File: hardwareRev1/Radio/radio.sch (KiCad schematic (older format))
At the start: 38 parts

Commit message: finaly back on track
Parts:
- removed C?: 2.2pf, symbol C
- removed C?: 22pf, symbol C
- removed C?: 33pf, symbol C
- removed C?: 47pf, symbol C
- removed C?: 15pf, symbol C
- removed C?: 4.7pf, symbol C
- removed C?: 1.8pf, symbol C
- removed C? (x4): C, symbol C
- removed L?: 150nh, symbol INDUCTOR
- removed L?: 120nH, symbol INDUCTOR
- removed L?: 39nH, symbol INDUCTOR
- removed L?: 47nH, symbol INDUCTOR
- removed L?: INDUCTOR, symbol INDUCTOR
- removed R?: R, symbol R
- removed U?: RF5110G, MODULE, symbol RF5110G
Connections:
- wire segments 107 -> 68

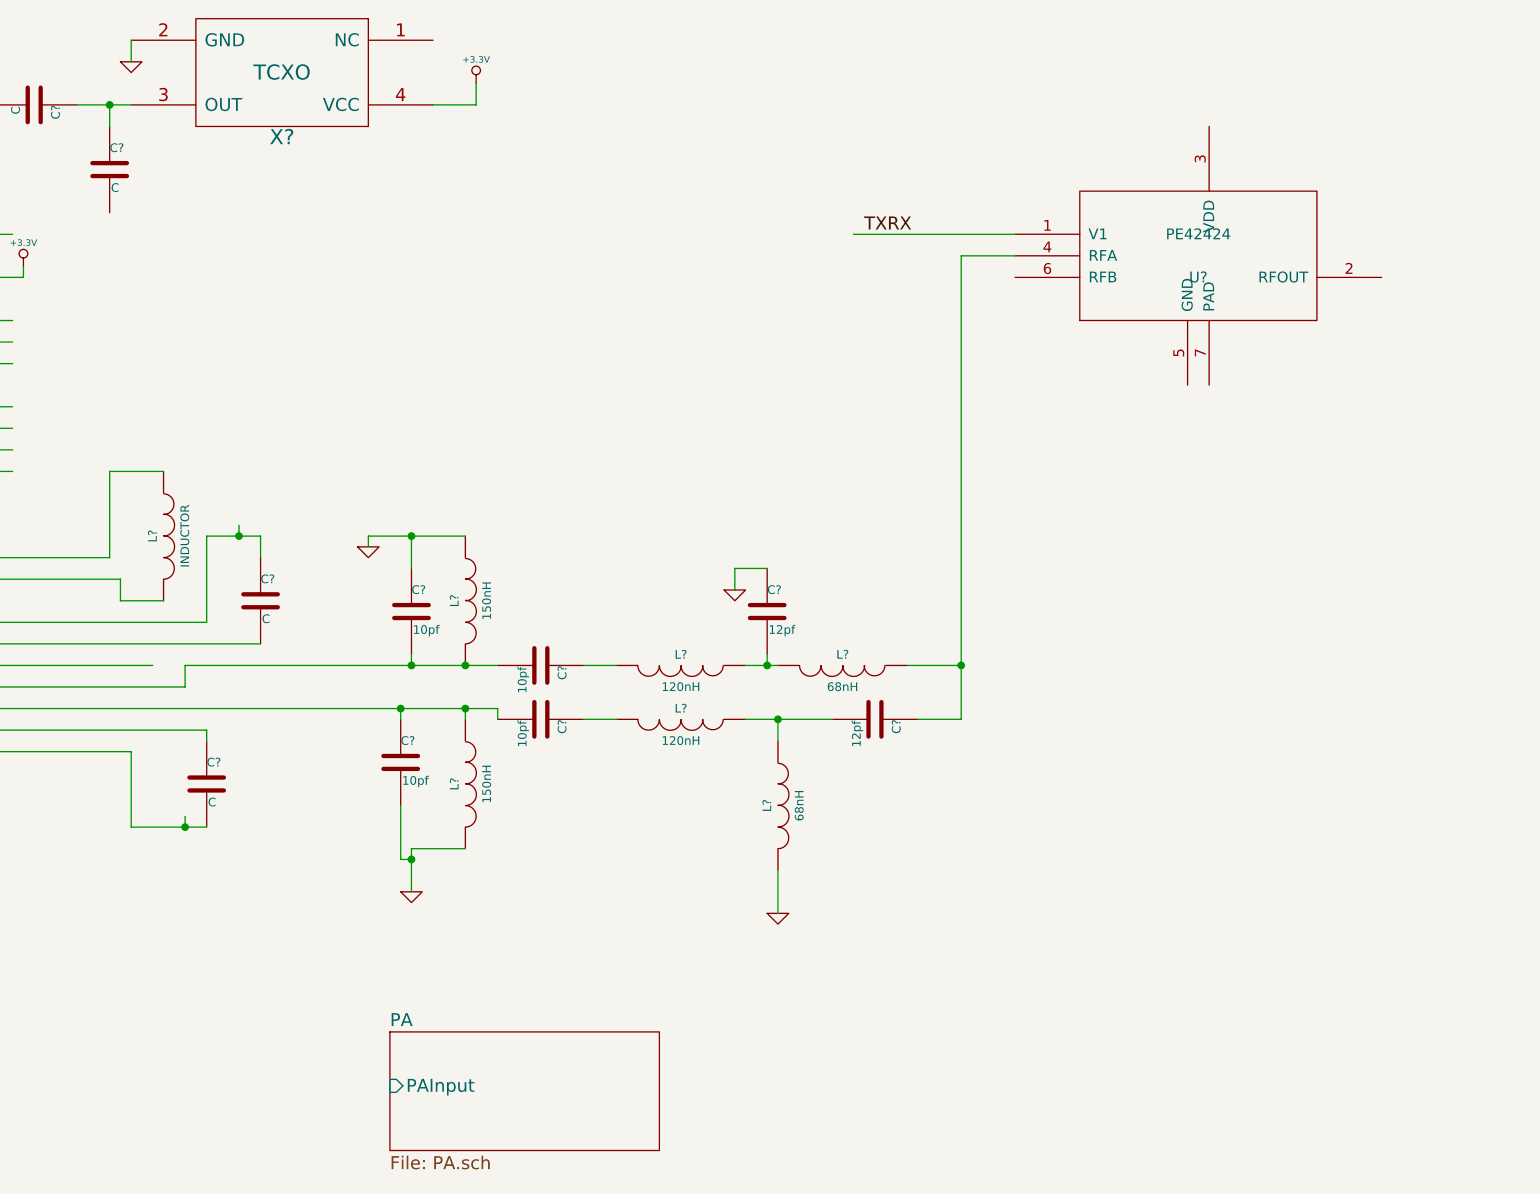
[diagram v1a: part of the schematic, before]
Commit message: Added the outline for the RF module. Also finished the schematic.
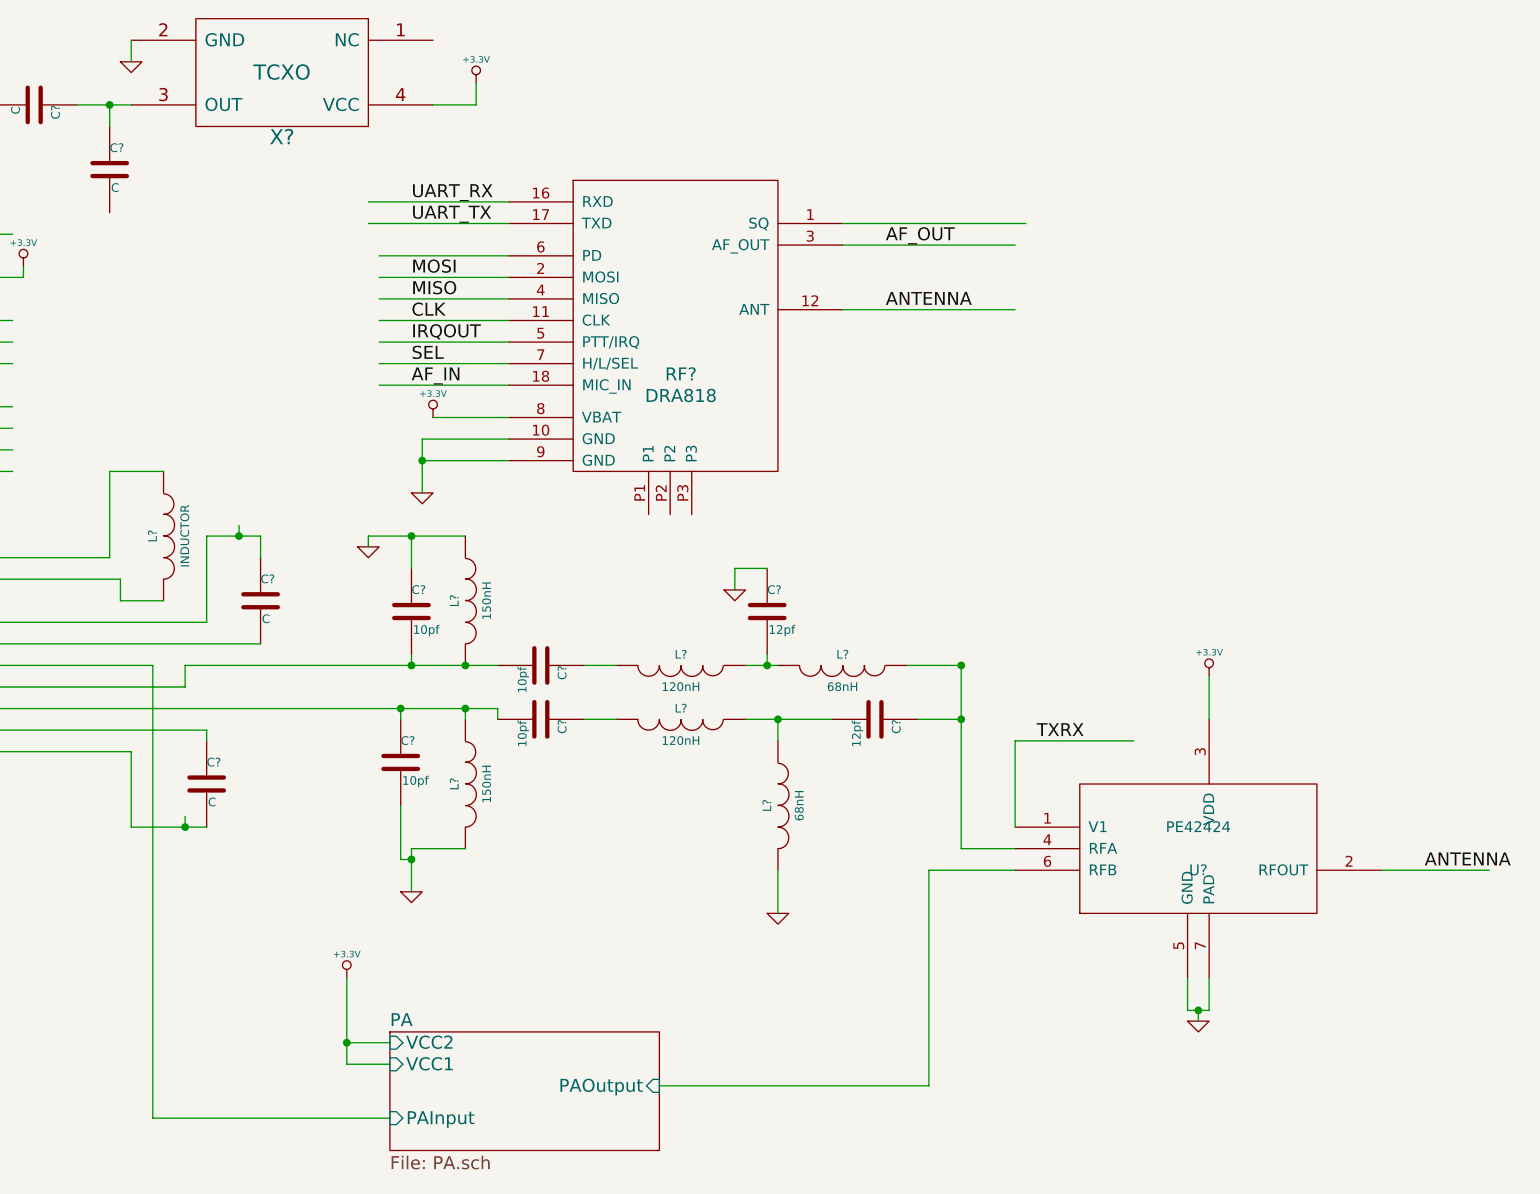
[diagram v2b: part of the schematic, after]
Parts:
- added RF?: DRA818, symbol DRA818
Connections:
- net labels added: ANTENNA
- wire segments 68 -> 99
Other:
- moved on the sheet: U?

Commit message: added the radio .
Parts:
- added C34: 1uf, Capacitors_SMD:C_0402, symbol C
- added C35: 100pf, Capacitors_SMD:C_0402, symbol C
- C1, C10, C2, C3, C4, C5, C6, C7, C8, C9: renamed from C?; footprint (none) -> Capacitors_SMD:C_0402
- L1: renamed from L?; value INDUCTOR -> 60nh; footprint (none) -> Resistors_SMD:R_0402
- L2, L3, L4, L5, L6, L7: renamed from L?; footprint (none) -> Resistors_SMD:R_0402
- RF1: renamed from RF?; footprint (none) -> hardwareRev1:RFModuleOutline
- U1: renamed from U?; footprint MODULE -> w_smd_qfn:qfn-28
- U2: renamed from U?; footprint MODULE -> hardwareRev1:PE4242
- X1: renamed from X?; footprint (none) -> hardwareRev1:FOX924B
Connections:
- net labels removed: ANTENNA
- wire segments 99 -> 113
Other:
- moved on the sheet: C1, C2

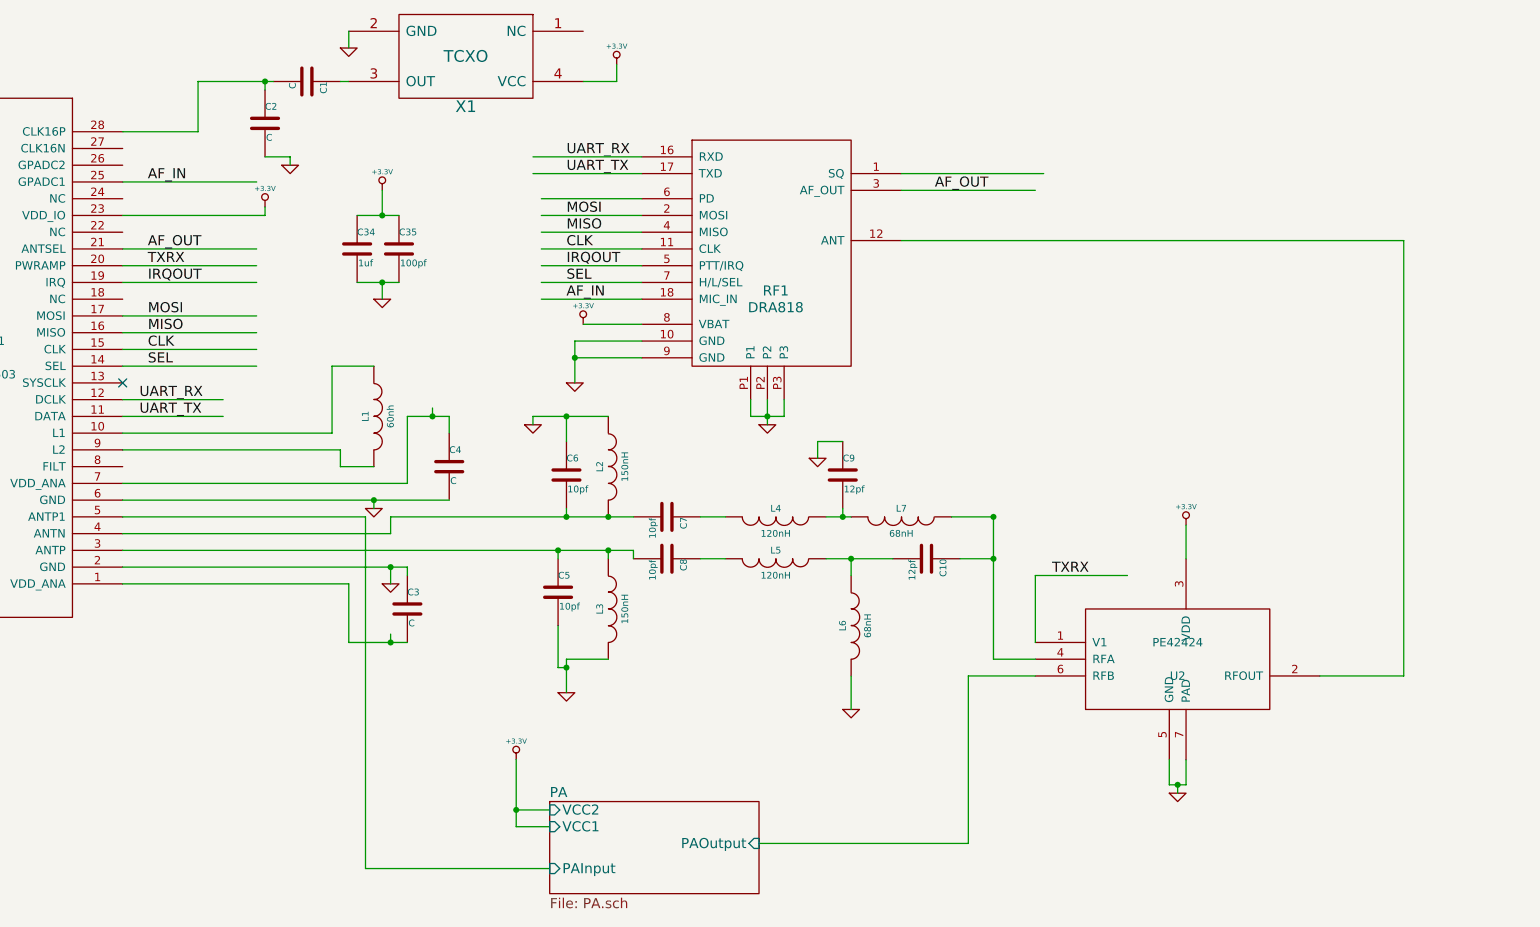
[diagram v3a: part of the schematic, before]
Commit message: Finished the PCB for the new radio module.
Still needs to be checked.
Added the datasheet for the amp and switch
Added the footprint for a 1.27mm pitch 2X8 connector
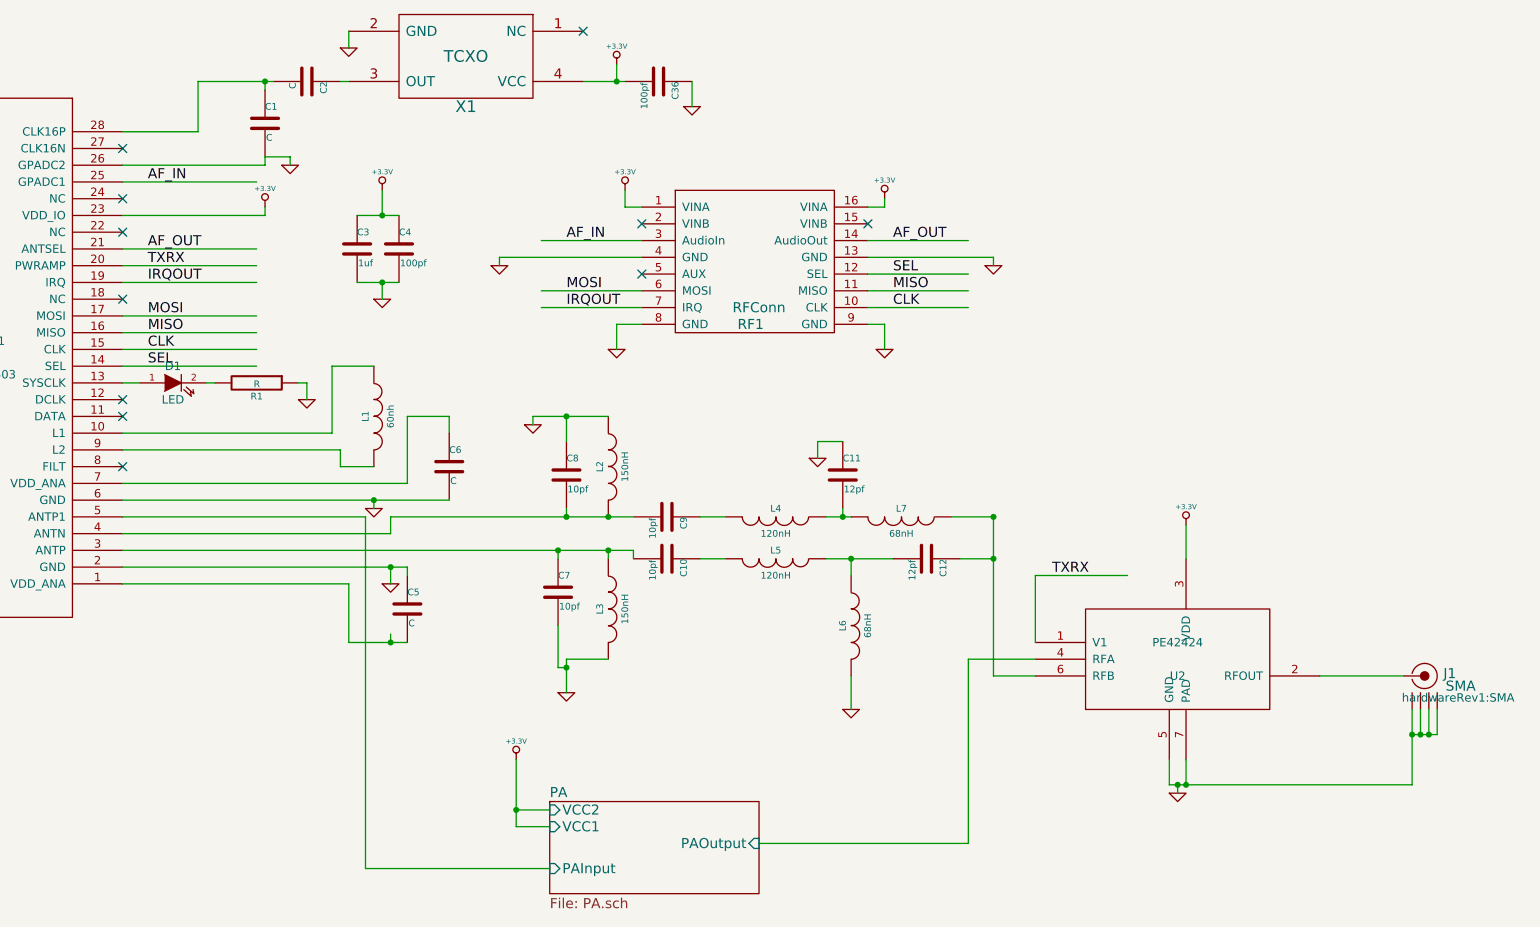
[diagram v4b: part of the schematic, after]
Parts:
- removed RF1: DRA818, hardwareRev1:RFModuleOutline, symbol DRA818
- added C36: 100pf, Capacitors_SMD:C_0402, symbol C
- added D1: LED, LEDs:LED-0603, symbol LED
- added J1: SMA, hardwareRev1:SMA, symbol SMA
- added R1: R, Resistors_SMD:R_0402, symbol R
- added RF1: RFConn, hardwareRev1:1.27mm2X8, symbol RFConn
- U1: footprint w_smd_qfn:qfn-28 -> Housings_DFN_QFN:QFN-28-1EP_5x5mm_Pitch0.5mm
- renumbered C2 to C1, C8 to C10, C9 to C11, C10 to C12, C1 to C2, C34 to C3, C35 to C4, C3 to C5, C4 to C6, C5 to C7, C6 to C8, C7 to C9
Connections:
- net labels removed: UART_RX, UART_TX
- wire segments 113 -> 120
- no-connect marks 1 -> 11

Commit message: Rerouted some power traces. Need to rerout it again.
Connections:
- net labels added: DATA, Data
- wire segments 120 -> 122
- no-connect marks 11 -> 9
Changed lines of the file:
@@
 $EndComp
 $Comp
-L GND #PWR01
+L GND #PWR13
 U 1 1 55504E95
 P 4300 4600
-F 0 "#PWR01" H 4300 4600 30  0001 C CNN
+F 0 "#PWR13" H 4300 4600 30  0001 C CNN
 F 1 "GND" H 4300 4530 30  0001 C CNN
 F 2 "" H 4300 4600 60  0000 C CNN
@@
 $EndComp
 $Comp
-L GND #PWR02
+L GND #PWR19
 U 1 1 55504EC1
 P 6000 4700
-F 0 "#PWR02" H 6000 4700 30  0001 C CNN
+F 0 "#PWR19" H 6000 4700 30  0001 C CNN
 F 1 "GND" H 6000 4630 30  0001 C CNN
 F 2 "" H 6000 4700 60  0000 C CNN
@@
 $EndComp
 $Comp
-L GND #PWR03
+L GND #PWR18
 U 1 1 55504EED
 P 5800 3200
-F 0 "#PWR03" H 5800 3200 30  0001 C CNN
+F 0 "#PWR18" H 5800 3200 30  0001 C CNN
 F 1 "GND" H 5800 3130 30  0001 C CNN
 F 2 "" H 5800 3200 60  0000 C CNN
@@
 $EndComp
 $Comp
-L GND #PWR04
+L GND #PWR12
 U 1 1 55504F19
 P 4100 3000
-F 0 "#PWR04" H 4100 3000 30  0001 C CNN
+F 0 "#PWR12" H 4100 3000 30  0001 C CNN
 F 1 "GND" H 4100 2930 30  0001 C CNN
 F 2 "" H 4100 3000 60  0000 C CNN
@@
 AF_IN
 $Comp
-L +3.3V #PWR05
+L +3.3V #PWR2
 U 1 1 55507330
 P 2500 1700
-F 0 "#PWR05" H 2500 1660 30  0001 C CNN
+F 0 "#PWR2" H 2500 1660 30  0001 C CNN
 F 1 "+3.3V" H 2500 1810 30  0000 C CNN
 F 2 "" H 2500 1700 60  0000 C CNN
@@
 $EndComp
 $Comp
-L +3.3V #PWR06
+L +3.3V #PWR14
 U 1 1 55507690
 P 4600 850
-F 0 "#PWR06" H 4600 810 30  0001 C CNN
+F 0 "#PWR14" H 4600 810 30  0001 C CNN
 F 1 "+3.3V" H 4600 960 30  0000 C CNN
 F 2 "" H 4600 850 60  0000 C CNN
@@
 $EndComp
 $Comp
-L GND #PWR07
+L GND #PWR5
 U 1 1 555076C0
 P 3000 750
-F 0 "#PWR07" H 3000 750 30  0001 C CNN
+F 0 "#PWR5" H 3000 750 30  0001 C CNN
 F 1 "GND" H 3000 680 30  0001 C CNN
 F 2 "" H 3000 750 60  0000 C CNN
@@
 $EndSheet
 $Comp
-L +3.3V #PWR08
+L +3.3V #PWR11
 U 1 1 55516AC2
 P 4000 5000
-F 0 "#PWR08" H 4000 4960 30  0001 C CNN
+F 0 "#PWR11" H 4000 4960 30  0001 C CNN
 F 1 "+3.3V" H 4000 5110 30  0000 C CNN
 F 2 "" H 4000 5000 60  0000 C CNN
@@
 $EndComp
 $Comp
-L GND #PWR09
+L GND #PWR23
 U 1 1 55517E5E
 P 7950 5200
-F 0 "#PWR09" H 7950 5200 30  0001 C CNN
+F 0 "#PWR23" H 7950 5200 30  0001 C CNN
 F 1 "GND" H 7950 5130 30  0001 C CNN
 F 2 "" H 7950 5200 60  0000 C CNN
@@
 $EndComp
 $Comp
-L +3.3V #PWR010
+L +3.3V #PWR24
 U 1 1 55518491
 P 8000 3600
-F 0 "#PWR010" H 8000 3560 30  0001 C CNN
+F 0 "#PWR24" H 8000 3560 30  0001 C CNN
 F 1 "+3.3V" H 8000 3710 30  0000 C CNN
 F 2 "" H 8000 3600 60  0000 C CNN
@@
 $EndComp
 $Comp
-L GND #PWR011
+L GND #PWR8
 U 1 1 55516403
 P 3200 2250
-F 0 "#PWR011" H 3200 2250 30  0001 C CNN
+F 0 "#PWR8" H 3200 2250 30  0001 C CNN
 F 1 "GND" H 3200 2180 30  0001 C CNN
 F 2 "" H 3200 2250 60  0000 C CNN
@@
 $EndComp
 $Comp
-L +3.3V #PWR012
+L +3.3V #PWR7
 U 1 1 5551643A
 P 3200 1600
-F 0 "#PWR012" H 3200 1560 30  0001 C CNN
+F 0 "#PWR7" H 3200 1560 30  0001 C CNN
 F 1 "+3.3V" H 3200 1710 30  0000 C CNN
 F 2 "" H 3200 1600 60  0000 C CNN
@@
 Connection ~ 3200 1750
 $Comp
-L GND #PWR013
+L GND #PWR3
 U 1 1 55517326
 P 2650 1450
-F 0 "#PWR013" H 2650 1450 30  0001 C CNN
+F 0 "#PWR3" H 2650 1450 30  0001 C CNN
 F 1 "GND" H 2650 1380 30  0001 C CNN
 F 2 "" H 2650 1450 60  0000 C CNN
@@
 	2950 950  3000 950
 $Comp
-L GND #PWR014
+L GND #PWR1
 U 1 1 5551A2E5
 P 250 2300
-F 0 "#PWR014" H 250 2300 30  0001 C CNN
+F 0 "#PWR1" H 250 2300 30  0001 C CNN
 F 1 "GND" H 250 2230 30  0001 C CNN
 F 2 "" H 250 2300 60  0000 C CNN
@@
 	250  2300 250  2200
 $Comp
-L GND #PWR015
+L GND #PWR9
 U 1 1 5551A717
 P 3250 3950
-F 0 "#PWR015" H 3250 3950 30  0001 C CNN
+F 0 "#PWR9" H 3250 3950 30  0001 C CNN
 F 1 "GND" H 3250 3880 30  0001 C CNN
 F 2 "" H 3250 3950 60  0000 C CNN
@@
 $EndComp
 $Comp
-L GND #PWR016
+L GND #PWR6
 U 1 1 5551A74E
 P 3150 3500
-F 0 "#PWR016" H 3150 3500 30  0001 C CNN
+F 0 "#PWR6" H 3150 3500 30  0001 C CNN
 F 1 "GND" H 3150 3430 30  0001 C CNN
 F 2 "" H 3150 3500 60  0000 C CNN
@@
 $EndComp
 $Comp
-L +3.3V #PWR017
+L +3.3V #PWR20
 U 1 1 55EDBB05
 P 6200 1650
-F 0 "#PWR017" H 6200 1610 30  0001 C CNN
+F 0 "#PWR20" H 6200 1610 30  0001 C CNN
 F 1 "+3.3V" H 6200 1760 30  0000 C CNN
 F 2 "" H 6200 1650 60  0000 C CNN
@@
 $EndComp
 $Comp
-L +3.3V #PWR018
+L +3.3V #PWR16
 U 1 1 55EDBB3E
 P 4650 1600
-F 0 "#PWR018" H 4650 1560 30  0001 C CNN
+F 0 "#PWR16" H 4650 1560 30  0001 C CNN
 F 1 "+3.3V" H 4650 1710 30  0000 C CNN
 F 2 "" H 4650 1600 60  0000 C CNN
@@
 $EndComp
 $Comp
-L GND #PWR019
+L GND #PWR15
 U 1 1 55EDBB77
 P 4600 2550
-F 0 "#PWR019" H 4600 2550 30  0001 C CNN
+F 0 "#PWR15" H 4600 2550 30  0001 C CNN
 F 1 "GND" H 4600 2480 30  0001 C CNN
 F 2 "" H 4600 2550 60  0000 C CNN
@@
 $EndComp
 $Comp
-L GND #PWR020
+L GND #PWR21
 U 1 1 55EDBBB0
 P 6200 2550
-F 0 "#PWR020" H 6200 2550 30  0001 C CNN
+F 0 "#PWR21" H 6200 2550 30  0001 C CNN
 F 1 "GND" H 6200 2480 30  0001 C CNN
 F 2 "" H 6200 2550 60  0000 C CNN
@@
 $EndComp
 $Comp
-L GND #PWR021
+L GND #PWR4
 U 1 1 55EDC519
 P 2750 2850
-F 0 "#PWR021" H 2750 2850 30  0001 C CNN
+F 0 "#PWR4" H 2750 2850 30  0001 C CNN
 F 1 "GND" H 2750 2780 30  0001 C CNN
 F 2 "" H 2750 2850 60  0000 C CNN
@@
 NoConn ~ 1650 3250
 NoConn ~ 1650 2850
-NoConn ~ 1650 2950
 Text Label 1800 1950 0    60   ~ 0
 AF_OUT
@@
 AF_OUT
 $Comp
-L GND #PWR022
+L GND #PWR22
 U 1 1 55EDDBFC
 P 6850 2050
-F 0 "#PWR022" H 6850 2050 30  0001 C CNN
+F 0 "#PWR22" H 6850 2050 30  0001 C CNN
 F 1 "GND" H 6850 1980 30  0001 C CNN
 F 2 "" H 6850 2050 60  0000 C CNN
@@
 $EndComp
 $Comp
-L GND #PWR023
+L GND #PWR10
 U 1 1 55EDDC47
 P 3900 2050
-F 0 "#PWR023" H 3900 2050 30  0001 C CNN
+F 0 "#PWR10" H 3900 2050 30  0001 C CNN
 F 1 "GND" H 3900 1980 30  0001 C CNN
 F 2 "" H 3900 2050 60  0000 C CNN
@@
 NoConn ~ 6100 1800
 NoConn ~ 4750 1800
-NoConn ~ 4750 2100
 $Comp
 L C C36
@@
 $EndComp
 $Comp
-L GND #PWR024
+L GND #PWR17
 U 1 1 55EDB837
 P 5050 1100
-F 0 "#PWR024" H 5050 1100 30  0001 C CNN
+F 0 "#PWR17" H 5050 1100 30  0001 C CNN
 F 1 "GND" H 5050 1030 30  0001 C CNN
 F 2 "" H 5050 1100 60  0000 C CNN
@@
 Wire Wire Line
 	6850 4500 7100 4500
+Wire Wire Line
+	1650 2950 2450 2950
+Text Label 1850 2950 0    60   ~ 0
+DATA
+Text Label 4300 2100 0    60   ~ 0
+Data
+Wire Wire Line
+	4100 2100 4750 2100
 $EndSCHEMATC
